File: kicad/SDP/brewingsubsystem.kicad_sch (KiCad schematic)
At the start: 19 parts

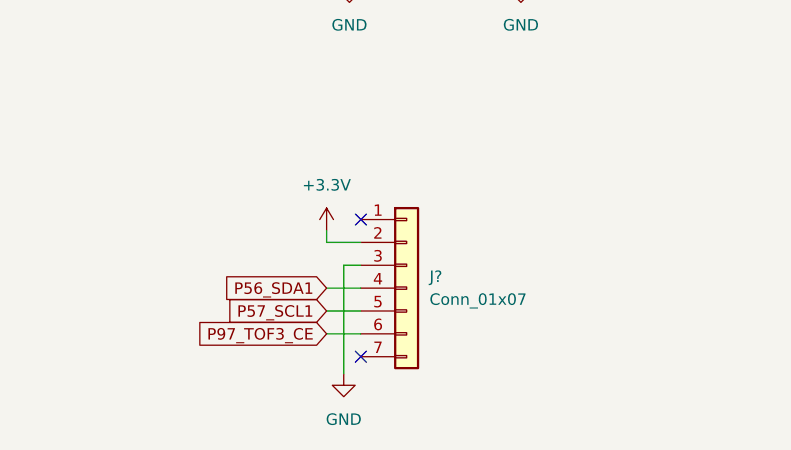
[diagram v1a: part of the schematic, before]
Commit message: Added GPIO headers, separated power PCB
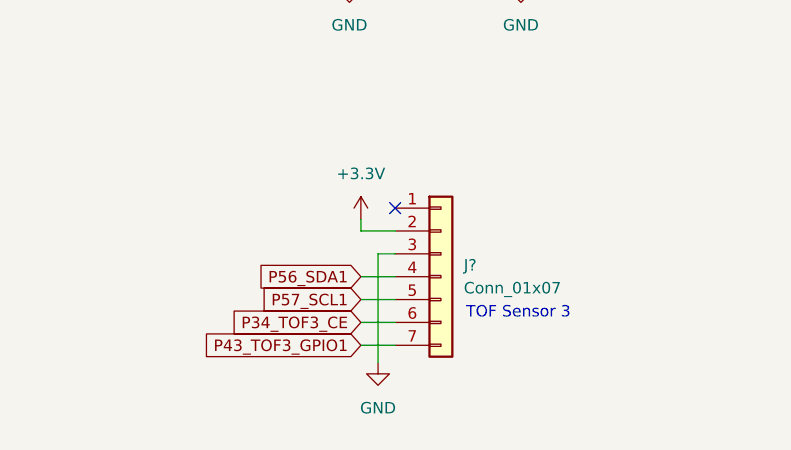
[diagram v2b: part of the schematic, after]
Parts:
- removed J?: Conn_01x07, symbol Connector_Generic:Conn_01x07
- added J?: Conn_01x07, symbol Connector_Generic:Conn_01x07
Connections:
- net +3V3: now also J?.2 (Pin_2)
- net GND: now also J?.3 (Pin_3)
- net P56_SDA1: now also J?.4 (Pin_4)
- net P57_SCL1: now also J?.5 (Pin_5)
- new net P34_TOF3_CE: J?.6 (Pin_6)
- new net P43_TOF3_GPIO1: J?.7 (Pin_7)
- no-connect marks 2 -> 1
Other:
- note added: "TOF Sensor 3"

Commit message: Added footprints
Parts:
- gave numbers to parts that had none: 19
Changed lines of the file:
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@@
   (symbol (lib_id "Jumper:Jumper_2_Open") (at 128.27 77.47 0) (unit 1)
     (in_bom yes) (on_board yes) (fields_autoplaced)
-    (property "Reference" "JP?" (id 0) (at 128.27 71.12 0))
+    (property "Reference" "JP18" (id 0) (at 128.27 71.12 0))
     (property "Value" "JP_MS3" (id 1) (at 128.27 73.66 0))
     (property "Footprint" "" (id 2) (at 128.27 77.47 0)
@@
   (symbol (lib_id "Connector_Generic:Conn_01x04") (at 176.53 52.07 0) (unit 1)
     (in_bom yes) (on_board yes) (fields_autoplaced)
-    (property "Reference" "J?" (id 0) (at 179.07 52.0699 0)
+    (property "Reference" "J20" (id 0) (at 179.07 52.0699 0)
       (effects (font (size 1.27 1.27)) (justify left))
     )
@@
   (symbol (lib_id "Connector_Generic:Conn_01x07") (at 67.31 109.22 0) (unit 1)
     (in_bom yes) (on_board yes) (fields_autoplaced)
-    (property "Reference" "J?" (id 0) (at 69.85 107.9499 0)
+    (property "Reference" "J21" (id 0) (at 69.85 107.9499 0)
       (effects (font (size 1.27 1.27)) (justify left))
     )
@@
   (symbol (lib_id "Device:R_Small") (at 143.51 72.39 180) (unit 1)
     (in_bom yes) (on_board yes) (fields_autoplaced)
-    (property "Reference" "R?" (id 0) (at 146.05 71.1199 0)
+    (property "Reference" "R39" (id 0) (at 146.05 71.1199 0)
       (effects (font (size 1.27 1.27)) (justify right))
     )
@@
   (symbol (lib_id "Device:R_Small") (at 134.62 33.02 0) (unit 1)
     (in_bom yes) (on_board yes) (fields_autoplaced)
-    (property "Reference" "R?" (id 0) (at 137.16 31.7499 0)
+    (property "Reference" "R37" (id 0) (at 137.16 31.7499 0)
       (effects (font (size 1.27 1.27)) (justify left))
     )
@@
   (symbol (lib_id "Jumper:Jumper_2_Open") (at 41.91 59.69 0) (unit 1)
     (in_bom yes) (on_board yes) (fields_autoplaced)
-    (property "Reference" "JP?" (id 0) (at 41.91 53.34 0))
+    (property "Reference" "JP13" (id 0) (at 41.91 53.34 0))
     (property "Value" "JP_MS1" (id 1) (at 41.91 55.88 0))
     (property "Footprint" "" (id 2) (at 41.91 59.69 0)
@@
   (symbol (lib_id "Driver_Motor:Pololu_Breakout_A4988") (at 157.48 52.07 0) (unit 1)
     (in_bom yes) (on_board yes)
-    (property "Reference" "A?" (id 0) (at 170.18 66.04 0)
+    (property "Reference" "A6" (id 0) (at 170.18 66.04 0)
       (effects (font (size 1.27 1.27)) (justify left))
     )
@@
   (symbol (lib_id "Device:C_Small") (at 172.72 34.29 0) (unit 1)
     (in_bom yes) (on_board yes) (fields_autoplaced)
-    (property "Reference" "C?" (id 0) (at 175.26 33.0262 0)
+    (property "Reference" "C35" (id 0) (at 175.26 33.0262 0)
       (effects (font (size 1.27 1.27)) (justify left))
     )
@@
   (symbol (lib_id "Device:R_Small") (at 48.26 33.02 0) (unit 1)
     (in_bom yes) (on_board yes) (fields_autoplaced)
-    (property "Reference" "R?" (id 0) (at 50.8 31.7499 0)
+    (property "Reference" "R35" (id 0) (at 50.8 31.7499 0)
       (effects (font (size 1.27 1.27)) (justify left))
     )
@@
   (symbol (lib_id "Device:R_Small") (at 39.37 33.02 0) (unit 1)
     (in_bom yes) (on_board yes) (fields_autoplaced)
-    (property "Reference" "R?" (id 0) (at 41.91 31.7499 0)
+    (property "Reference" "R34" (id 0) (at 41.91 31.7499 0)
       (effects (font (size 1.27 1.27)) (justify left))
     )
@@
   (symbol (lib_id "Device:C_Small") (at 86.36 34.29 0) (unit 1)
     (in_bom yes) (on_board yes) (fields_autoplaced)
-    (property "Reference" "C?" (id 0) (at 88.9 33.0262 0)
+    (property "Reference" "C34" (id 0) (at 88.9 33.0262 0)
       (effects (font (size 1.27 1.27)) (justify left))
     )
@@
   (symbol (lib_id "Driver_Motor:Pololu_Breakout_A4988") (at 71.12 52.07 0) (unit 1)
     (in_bom yes) (on_board yes)
-    (property "Reference" "A?" (id 0) (at 83.82 66.04 0)
+    (property "Reference" "A5" (id 0) (at 83.82 66.04 0)
       (effects (font (size 1.27 1.27)) (justify left))
     )
@@
   (symbol (lib_id "Jumper:Jumper_2_Open") (at 128.27 59.69 0) (unit 1)
     (in_bom yes) (on_board yes) (fields_autoplaced)
-    (property "Reference" "JP?" (id 0) (at 128.27 53.34 0))
+    (property "Reference" "JP14" (id 0) (at 128.27 53.34 0))
     (property "Value" "JP_MS1" (id 1) (at 128.27 55.88 0))
     (property "Footprint" "" (id 2) (at 128.27 59.69 0)
@@
   (symbol (lib_id "Device:R_Small") (at 125.73 33.02 0) (unit 1)
     (in_bom yes) (on_board yes) (fields_autoplaced)
-    (property "Reference" "R?" (id 0) (at 128.27 31.7499 0)
+    (property "Reference" "R36" (id 0) (at 128.27 31.7499 0)
       (effects (font (size 1.27 1.27)) (justify left))
     )
@@
   (symbol (lib_id "Jumper:Jumper_2_Open") (at 41.91 68.58 0) (unit 1)
     (in_bom yes) (on_board yes) (fields_autoplaced)
-    (property "Reference" "JP?" (id 0) (at 41.91 62.23 0))
+    (property "Reference" "JP15" (id 0) (at 41.91 62.23 0))
     (property "Value" "JP_MS2" (id 1) (at 41.91 64.77 0))
     (property "Footprint" "" (id 2) (at 41.91 68.58 0)
@@
   (symbol (lib_id "Jumper:Jumper_2_Open") (at 128.27 68.58 0) (unit 1)
     (in_bom yes) (on_board yes) (fields_autoplaced)
-    (property "Reference" "JP?" (id 0) (at 128.27 62.23 0))
+    (property "Reference" "JP16" (id 0) (at 128.27 62.23 0))
     (property "Value" "JP_MS2" (id 1) (at 128.27 64.77 0))
     (property "Footprint" "" (id 2) (at 128.27 68.58 0)
@@
   (symbol (lib_id "Jumper:Jumper_2_Open") (at 41.91 77.47 0) (unit 1)
     (in_bom yes) (on_board yes) (fields_autoplaced)
-    (property "Reference" "JP?" (id 0) (at 41.91 71.12 0))
+    (property "Reference" "JP17" (id 0) (at 41.91 71.12 0))
     (property "Value" "JP_MS3" (id 1) (at 41.91 73.66 0))
     (property "Footprint" "" (id 2) (at 41.91 77.47 0)
@@
   (symbol (lib_id "Connector_Generic:Conn_01x04") (at 90.17 52.07 0) (unit 1)
     (in_bom yes) (on_board yes) (fields_autoplaced)
-    (property "Reference" "J?" (id 0) (at 92.71 52.0699 0)
+    (property "Reference" "J19" (id 0) (at 92.71 52.0699 0)
       (effects (font (size 1.27 1.27)) (justify left))
     )
@@
   (symbol (lib_id "Device:R_Small") (at 57.15 72.39 180) (unit 1)
     (in_bom yes) (on_board yes) (fields_autoplaced)
-    (property "Reference" "R?" (id 0) (at 59.69 71.1199 0)
+    (property "Reference" "R38" (id 0) (at 59.69 71.1199 0)
       (effects (font (size 1.27 1.27)) (justify right))
     )

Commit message: Added footprints
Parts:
- C34, C35: footprint (none) -> footprints:50TZV100M8X10.5
- R34, R35, R36, R37, R38, R39: footprint (none) -> Resistor_SMD:R_0805_2012Metric
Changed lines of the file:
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@@
       (effects (font (size 1.27 1.27)) (justify right))
     )
-    (property "Footprint" "" (id 2) (at 143.51 72.39 0)
+    (property "Footprint" "Resistor_SMD:R_0805_2012Metric" (id 2) (at 143.51 72.39 0)
       (effects (font (size 1.27 1.27)) hide)
     )
@@
       (effects (font (size 1.27 1.27)) (justify left))
     )
-    (property "Footprint" "" (id 2) (at 134.62 33.02 0)
+    (property "Footprint" "Resistor_SMD:R_0805_2012Metric" (id 2) (at 134.62 33.02 0)
       (effects (font (size 1.27 1.27)) hide)
     )
@@
       (effects (font (size 1.27 1.27)) (justify left))
     )
-    (property "Footprint" "" (id 2) (at 172.72 34.29 0)
+    (property "Footprint" "footprints:50TZV100M8X10.5" (id 2) (at 172.72 34.29 0)
       (effects (font (size 1.27 1.27)) hide)
     )
@@
       (effects (font (size 1.27 1.27)) (justify left))
     )
-    (property "Footprint" "" (id 2) (at 48.26 33.02 0)
+    (property "Footprint" "Resistor_SMD:R_0805_2012Metric" (id 2) (at 48.26 33.02 0)
       (effects (font (size 1.27 1.27)) hide)
     )
@@
       (effects (font (size 1.27 1.27)) (justify left))
     )
-    (property "Footprint" "" (id 2) (at 39.37 33.02 0)
+    (property "Footprint" "Resistor_SMD:R_0805_2012Metric" (id 2) (at 39.37 33.02 0)
       (effects (font (size 1.27 1.27)) hide)
     )
@@
       (effects (font (size 1.27 1.27)) (justify left))
     )
-    (property "Footprint" "" (id 2) (at 86.36 34.29 0)
+    (property "Footprint" "footprints:50TZV100M8X10.5" (id 2) (at 86.36 34.29 0)
       (effects (font (size 1.27 1.27)) hide)
     )
@@
       (effects (font (size 1.27 1.27)) (justify left))
     )
-    (property "Footprint" "" (id 2) (at 125.73 33.02 0)
+    (property "Footprint" "Resistor_SMD:R_0805_2012Metric" (id 2) (at 125.73 33.02 0)
       (effects (font (size 1.27 1.27)) hide)
     )
@@
       (effects (font (size 1.27 1.27)) (justify right))
     )
-    (property "Footprint" "" (id 2) (at 57.15 72.39 0)
-      (effects (font (size 1.27 1.27)) hide)
-    )
+    (property "Footprint" "Resistor_SMD:R_0805_2012Metric" (id 2) (at 57.15 72.39 0)
+      (effects (font (size 1.27 1.27)) hide)
+    )

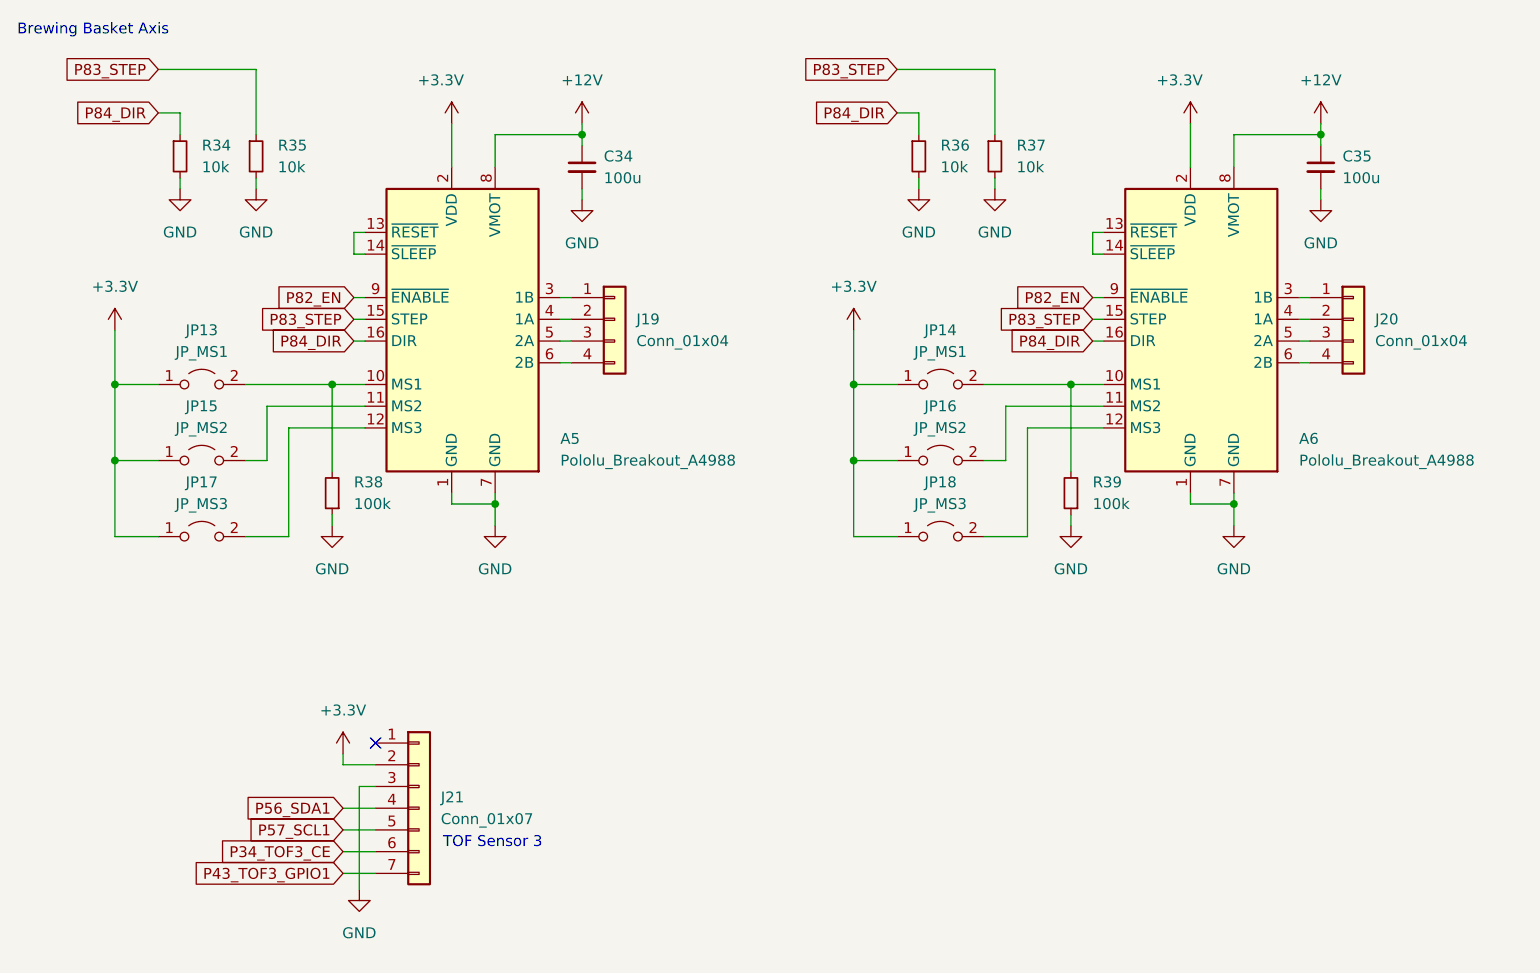
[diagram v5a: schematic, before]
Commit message: Assigned footprints, added limit switches, rearranged schematics
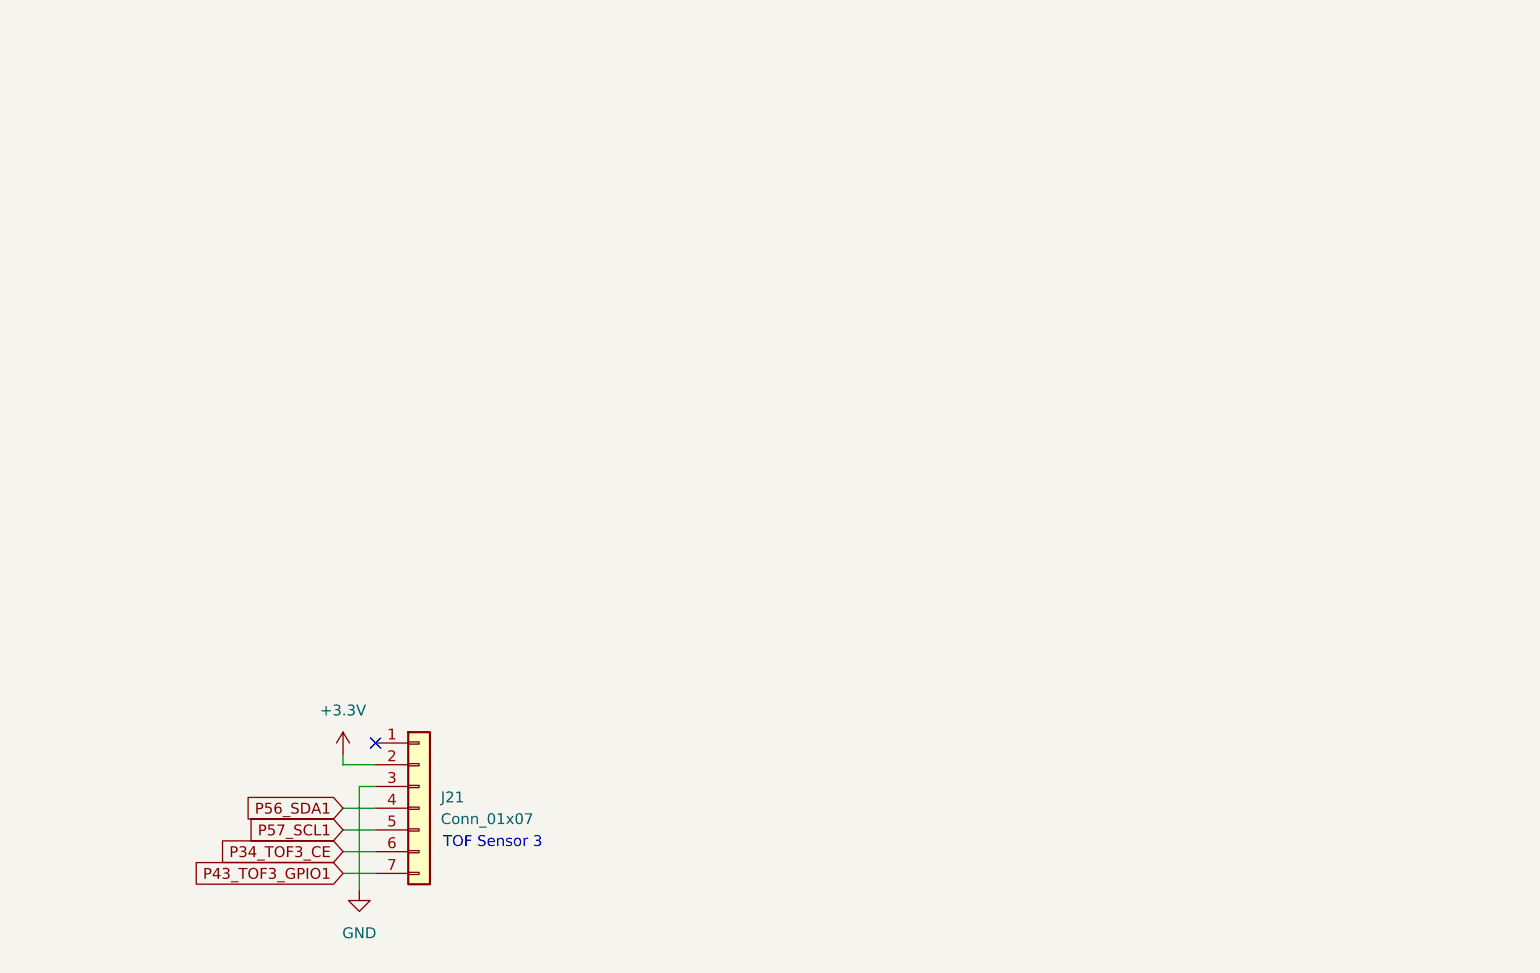
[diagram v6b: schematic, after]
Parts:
- removed A5, A6: Pololu_Breakout_A4988, Module:Pololu_Breakout-16_15.2x20.3mm, symbol Driver_Motor:Pololu_Breakout_A4988
- removed C34, C35: 100u, footprints:50TZV100M8X10.5, symbol Device:C_Small
- removed J19, J20: Conn_01x04, symbol Connector_Generic:Conn_01x04
- removed JP13, JP14: JP_MS1, symbol Jumper:Jumper_2_Open
- removed JP15, JP16: JP_MS2, symbol Jumper:Jumper_2_Open
- removed JP17, JP18: JP_MS3, symbol Jumper:Jumper_2_Open
- removed R34, R35, R36, R37: 10k, Resistor_SMD:R_0805_2012Metric, symbol Device:R_Small
- removed R38, R39: 100k, Resistor_SMD:R_0805_2012Metric, symbol Device:R_Small
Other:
- note removed: "Brewing Basket Axis"
